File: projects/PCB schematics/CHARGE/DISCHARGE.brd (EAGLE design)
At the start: 160 x 100 mm, 0 parts

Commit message: RTDS - Rev A.
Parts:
- added J1, J2: 770966-1, IowaFormula:CONN2_770966-1
- added R1, R2, R3, R4, R5, R6: 560, PF1262:TO126
- added U$1: PNC113, IowaFormula:PNC113
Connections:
- new net DISCHARGE_COIL+: U$1.X1
- new net DISCHARGE_COIL-: U$1.X2
- new net HEATSINK: R1.THERM, R2.THERM, R3.THERM, R4.THERM, R5.THERM, R6.THERM
- new net HV-: J2.1, J2.2, R6.1
- new net MOTORCONTROLLER+: J1.1, J1.2, R1.2
- new net N$1: R5.1, R6.2
- new net N$2: R4.1, R5.2
- new net N$3: R3.1, R4.2
- new net N$4: R2.1, R3.2
- new net N$5: R1.1, R2.2
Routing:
- net HEATSINK: track 0.00 -> 300.0 mm
- net N$3: track 0.00 -> 43.7 mm
- net N$2: track 0.00 -> 41.2 mm
- net N$4: track 0.00 -> 40.4 mm
- net MOTORCONTROLLER+: track 0.00 -> 23.4 mm
- net HV-: track 0.00 -> 21.8 mm
- net N$5: track 0.00 -> 15.2 mm
- net N$1: track 0.00 -> 15.2 mm
- added copper zone on layer 1, net HEATSINK
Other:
- board size 160 x 100 mm -> 99.1 x 99.1 mm
- board text added: "Author: github.com/michaelpass"
- board text added: "DISCHARGE Board Rev A: April 30th, 2019"
- board text added: "HV-"
- board text added: "Iowa Formula"
- board text added: "MOTORCONTROLLER+"

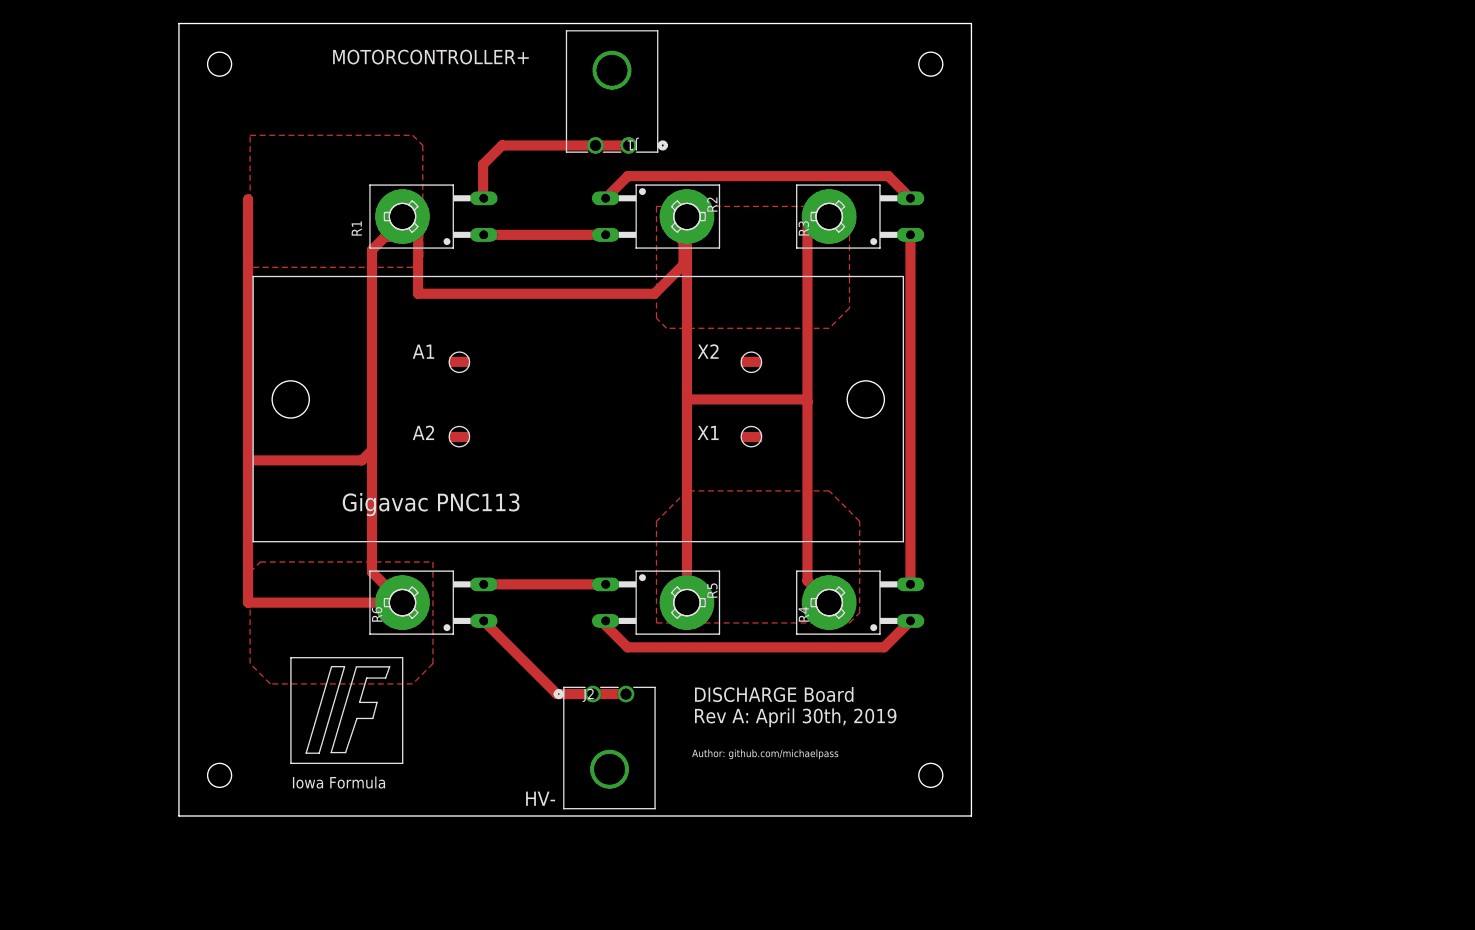
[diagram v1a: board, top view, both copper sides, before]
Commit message: POWER - DCDC changes w/ Ryan.
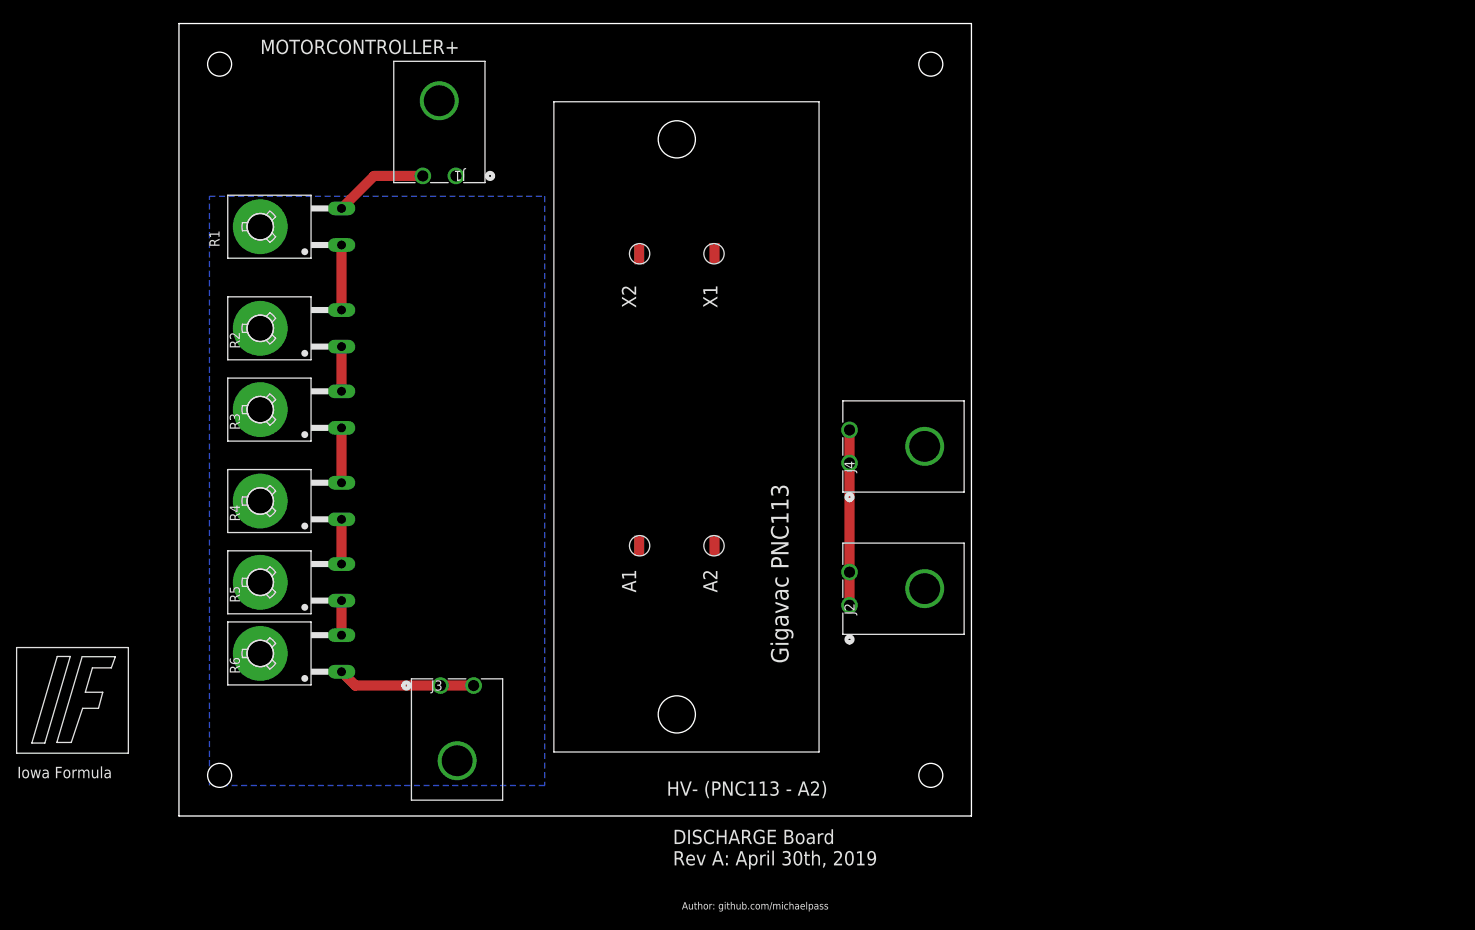
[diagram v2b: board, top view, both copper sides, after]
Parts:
- added J3, J4: 770966-1, IowaFormula:CONN2_770966-1
- moved R3 75.1 mm to (15.2, 50.8)
- moved R4 72.2 mm to (15.2, 39.4)
- moved U$1 62.3 mm to (62.2, 12.7), turned to 90 degrees
- moved R2 45.4 mm to (15.2, 61.0), turned to 90 degrees
- moved R5 43.3 mm to (15.2, 29.2), turned to 90 degrees
- moved J2 31.8 mm to (83.8, 30.5), turned to 90 degrees
- moved J1 21.9 mm to (30.5, 80.0)
- moved R6 18.9 mm to (15.2, 20.3)
- moved R1 17.8 mm to (15.2, 73.7)
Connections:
- new net POST_RESISTOR: J3.1, J3.2, R6.1
- net HV-: now also J4.1, J4.2; no longer R6.1
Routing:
- net HEATSINK: track 300.0 -> 0.00 mm
- net N$3: track 43.7 -> 6.86 mm
- net N$2: track 41.2 -> 5.59 mm
- net N$4: track 40.4 -> 5.33 mm
- net POST_RESISTOR: track 0.00 -> 17.2 mm
- net MOTORCONTROLLER+: track 23.4 -> 11.8 mm
- net N$1: track 15.2 -> 4.32 mm
- net N$5: track 15.2 -> 8.13 mm
- added copper zone on layer 16, net HEATSINK
- removed copper zone on layer 1, net HEATSINK
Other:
- board text added: "HV- (PNC113 - A2)"
- board text removed: "HV-"

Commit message: PROJ - Silkscreen modifications - 50%.
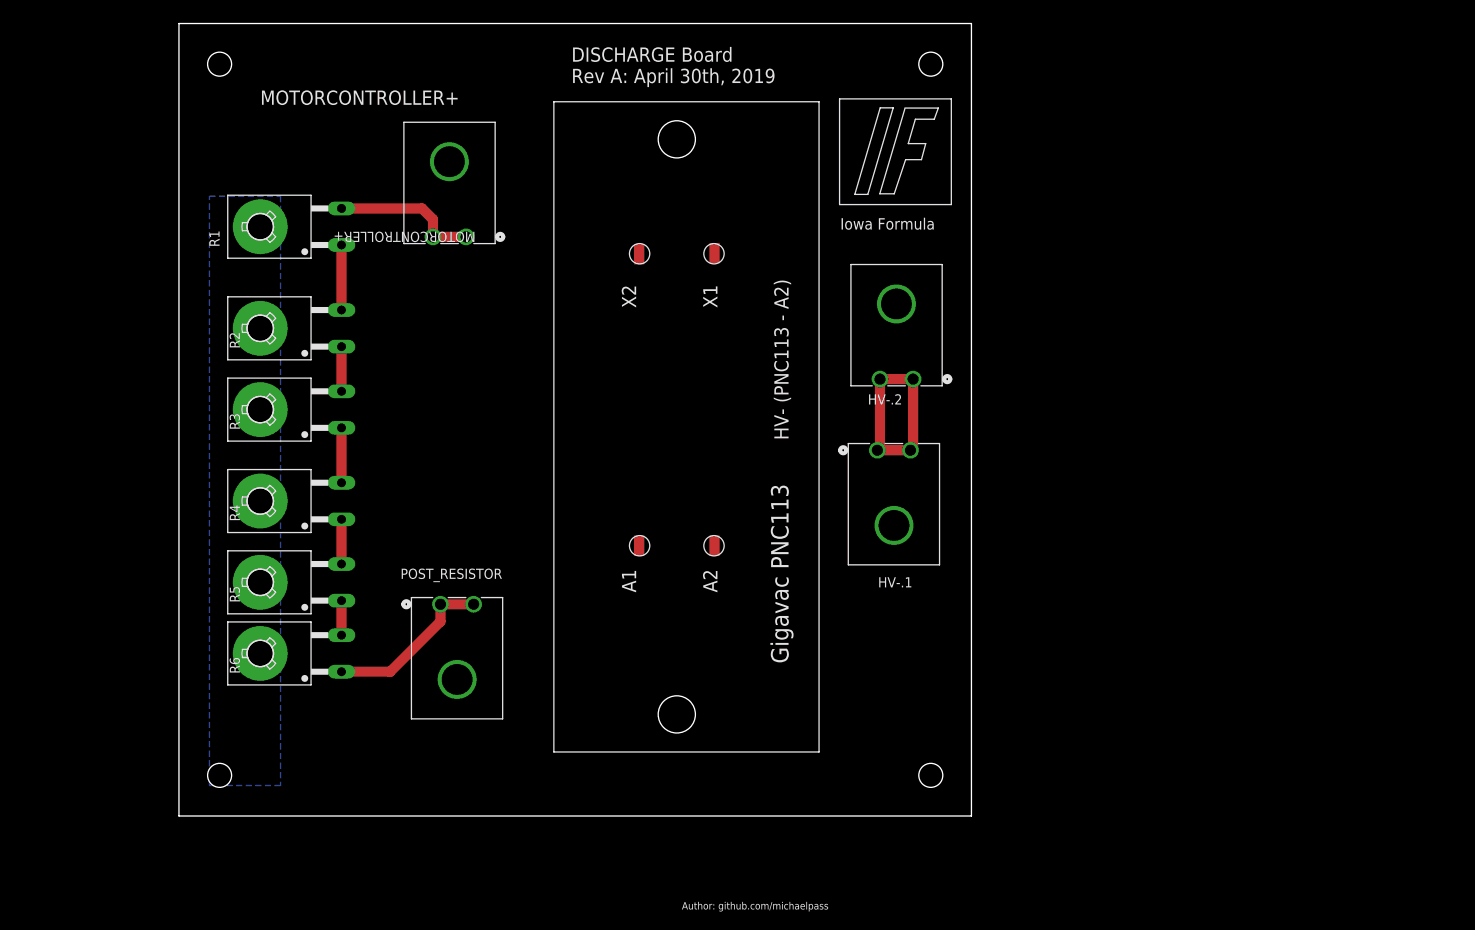
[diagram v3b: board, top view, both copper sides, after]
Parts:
- removed J1, J2, J3, J4: 770966-1, IowaFormula:CONN2_770966-1
- added HV-.1, HV-.2, MOTORCONTROLLER+, POST_RESISTOR: 770966-1, IowaFormula:CONN2_770966-1
- renumbered U$1 to PNC113
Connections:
- net HV-: now also HV-.1.1, HV-.1.2, HV-.2.1, HV-.2.2; no longer J2.1, J2.2, J4.1, J4.2
- net MOTORCONTROLLER+: now also MOTORCONTROLLER+.1, MOTORCONTROLLER+.2; no longer J1.1, J1.2
- net POST_RESISTOR: now also POST_RESISTOR.1, POST_RESISTOR.2; no longer J3.1, J3.2
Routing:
- net MOTORCONTROLLER+: track 11.8 -> 18.3 mm
- net HV-: track 21.9 -> 26.2 mm
- net POST_RESISTOR: track 17.2 -> 21.3 mm

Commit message: PROJ - Final pre-purchase revisions (4 boards still in progress.)
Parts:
- moved PNC113 2.54 mm to (59.7, 12.7)
- moved MOTORCONTROLLER+ 1.27 mm to (33.0, 72.4)
- moved POST_RESISTOR 1.27 mm to (38.1, 26.5)
- moved R1 1.27 mm to (16.5, 73.7)
- moved R2 1.27 mm to (16.5, 61.0)
- moved R3 1.27 mm to (16.5, 50.8)
- moved R4 1.27 mm to (16.5, 39.4)
- moved R5 1.27 mm to (16.5, 29.2)
- moved R6 1.27 mm to (16.5, 20.3)
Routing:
- added copper zone on layer 1, net HEATSINK
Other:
- board text added: "(To PNC113-A1)"
- board text added: "(To PNC113-A2)"
- board text added: "(To Vehicle)"
- board text added: "Connect X1 on PNC113 to (CHARGE) CHRGCTRL-, DISCHARGECOIL+: Pin 7"
- board text added: "Connect X2 on PNC113 to (CHARGE) CHRGCTRL-, DISCHARGECOIL-: Pin 6"

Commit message: PROJ - Gerber files major milestone - 05/05/19.
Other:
- board text added: "DISCHARGE Board Rev A: May 5th, 2019"
- board text removed: "DISCHARGE Board Rev A: April 30th, 2019"
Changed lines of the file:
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@@
 <hole x="5.08" y="93.98" drill="3"/>
 <text x="46.5074" y="90.3478" size="1.778" layer="25" font="vector">DISCHARGE Board
-Rev A: April 30th, 2019</text>
-<text x="62.865" y="-11.684" size="0.9144" layer="25">Author: github.com/michaelpass</text>
+Rev A: May 5th, 2019</text>
+<text x="66.675" y="3.556" size="0.9144" layer="25">Author: github.com/michaelpass</text>
 <wire x1="82.5754" y1="89.6366" x2="82.5754" y2="76.4286" width="0.1524" layer="25"/>
 <wire x1="82.5754" y1="76.4286" x2="96.5454" y2="76.4286" width="0.1524" layer="25"/>
@@
 <wire x1="87.63" y1="54.61" x2="91.7702" y2="54.61" width="1.27" layer="1"/>
 <wire x1="91.44" y1="45.72" x2="87.2998" y2="45.72" width="1.27" layer="1"/>
-<wire x1="91.7702" y1="54.61" x2="91.7702" y2="45.72" width="1.27" layer="1"/>
 <wire x1="87.63" y1="54.61" x2="87.63" y2="46.0502" width="1.27" layer="1"/>
 <wire x1="87.63" y1="46.0502" x2="87.2998" y2="45.72" width="1.27" layer="1"/>
+<wire x1="91.7702" y1="54.61" x2="91.7702" y2="46.0502" width="1.27" layer="1"/>
+<wire x1="91.7702" y1="46.0502" x2="91.44" y2="45.72" width="1.27" layer="1"/>
 </signal>
 <signal name="N$1">
